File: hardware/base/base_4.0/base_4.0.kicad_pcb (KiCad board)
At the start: 2 copper layers, 94.6 x 17 mm, 9 parts, among them IC1 single_pad_smd, IC2 single_pad_smd, J1 Conn 1, J2 Conn 2

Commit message: 3.0 and 3.5 base updated
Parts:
- removed GND (x2): single_pad_smd, cycfi_library:single-pad-3x2
- removed IC1, IC2, OC1, OC2: single_pad_smd, cycfi_library:single-pad-2x2-th
- added J3: Conn_01x03, cycfi_library:xr2-coil-connector, F.Cu at (125.0, 52.0)
- added J4: Conn_01x03, cycfi_library:xr2-coil-connector, F.Cu at (125.0, 58.5)
- moved J1 6.00 mm to (156.5, 55.2)
- moved J2 5.70 mm to (153.1, 55.2)
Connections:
- net /ic2 renamed /OC2
- net /oc1 renamed /OC1
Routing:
- net GND: track 100.3 -> 9.22 mm, vias 6 -> 2
- net /ic1: track 34.3 -> 0.00 mm
- net /OC2: track 16.2 -> 32.6 mm
- net /OC1: track 56.5 -> 42.8 mm
- net /IC1: track 0.00 -> 10.2 mm
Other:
- outline, holes or cut-outs redrawn
- board text removed: "IC1"
- board text removed: "IC2"
- board text removed: "OC1"
- board text removed: "OC2"

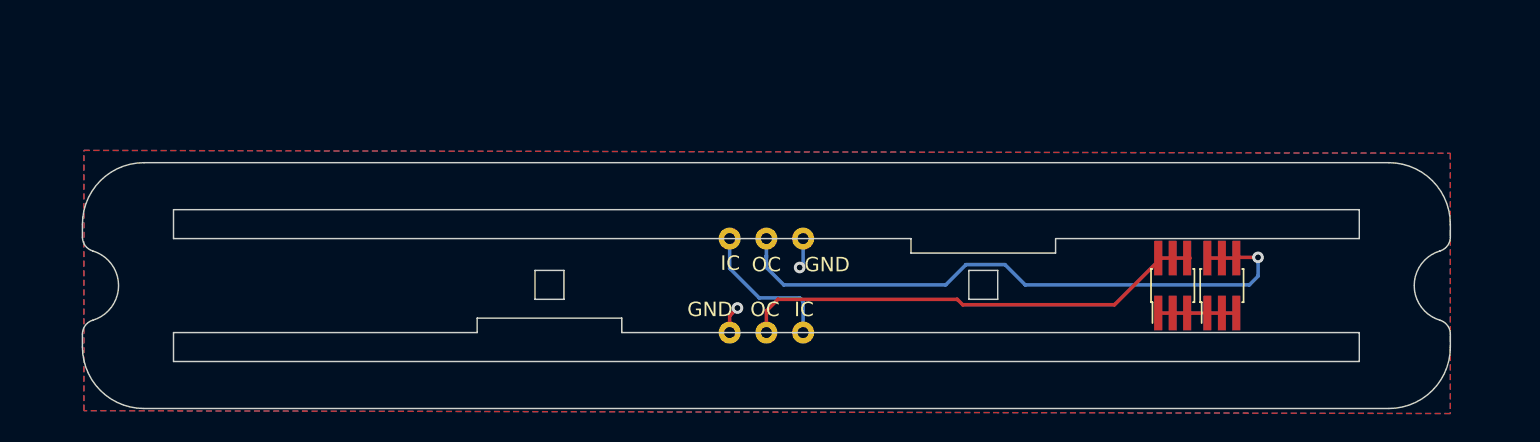
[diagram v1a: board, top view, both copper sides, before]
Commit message: Copied 3.3 to 3.5 and 4.0
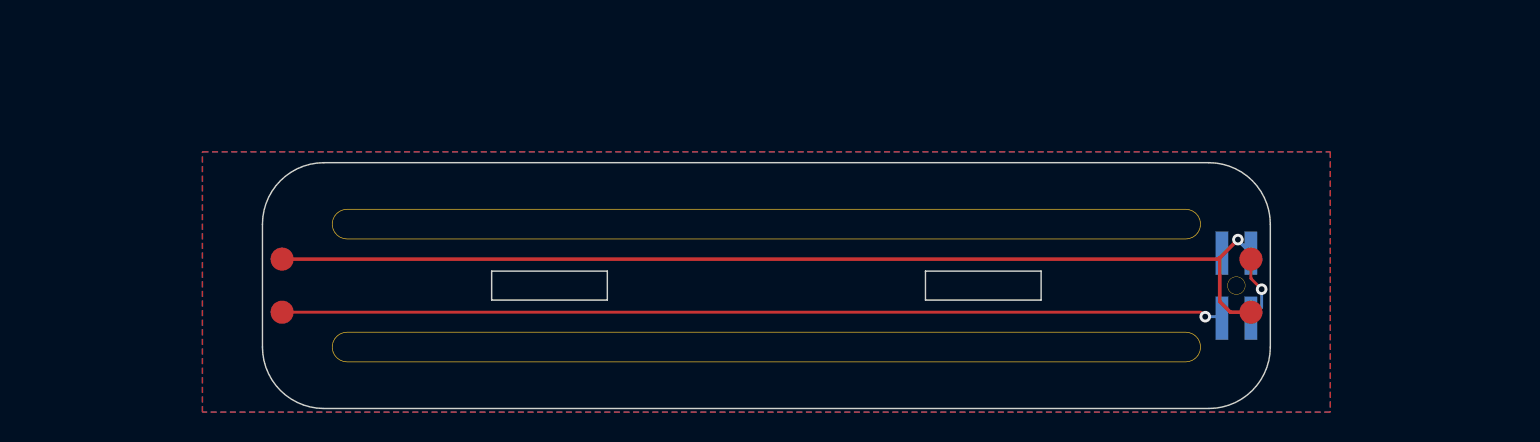
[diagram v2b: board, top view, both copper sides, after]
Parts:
- removed J2: Conn 2, cycfi_library:pin_header_2x3p_1.00mm_smd_vertical
- removed J3, J4: Conn_01x03, cycfi_library:xr2-coil-connector
- added H5: single_pad, xr_spectra_library:rail_slot_3.3, F.Cu at (125.0, 51.0)
- added H6: single_pad, xr_spectra_library:rail_slot_3.3, F.Cu at (125.0, 59.5)
- added IC1: single_pad, cycfi_library:single-pad-1.6x1.6_circular, F.Cu at (91.5, 53.4)
- added IC2: single_pad, cycfi_library:single-pad-1.6x1.6_circular, F.Cu at (158.5, 57.1)
- added OC1: single_pad, cycfi_library:single-pad-1.6x1.6_circular, F.Cu at (158.5, 53.4)
- added OC2: single_pad, cycfi_library:single-pad-1.6x1.6_circular, F.Cu at (91.5, 57.1)
- J1: value Conn 1 -> conn_2x2; footprint cycfi_library:pin_header_2x3p_1.00mm_smd_vertical -> cycfi_library:pin_header_2x2p_2.00mm_smd_vertical; moved to B.Cu
- moved J1 1.00 mm to (157.5, 55.2)
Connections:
- J1 pad 1: GND -> inner_coil
- J1 pad 3: GND -> /out-
- J1 pad 4: /OC1 -> /out+
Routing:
- net inner_coil: track 0.00 -> 73.4 mm, vias 0 -> 1
- net /out-: track 0.00 -> 65.2 mm, vias 0 -> 1
- net /OC1: track 42.8 -> 0.00 mm, vias 1 -> 0
- net /OC2: track 32.6 -> 0.00 mm
- net /IC1: track 10.2 -> 0.00 mm
- net GND: track 9.22 -> 0.00 mm, vias 2 -> 0
- net /out+: track 0.00 -> 4.70 mm, vias 0 -> 1
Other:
- board size 94.6 x 17 mm -> 69.7 x 17 mm
- net class Default removed

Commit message: WIP
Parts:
- added H1: MountingHole, cycfi_library:hole_3mm, F.Cu at (138.0, 39.0)
- added H2: MountingHole, cycfi_library:hole_3mm, F.Cu at (134.0, 39.0)
- H5, H6: footprint xr_spectra_library:rail_slot_3.3 -> xr_spectra_library:rail_slot_4.0
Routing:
- net inner_coil: track 73.4 -> 0.00 mm, vias 1 -> 0
- net /out-: track 65.2 -> 0.00 mm, vias 1 -> 0
- net /out+: track 4.70 -> 0.00 mm, vias 1 -> 0
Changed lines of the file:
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@@
   (footprint "cycfi_library:single-pad-1.6x1.6_circular" (layer "F.Cu")
     (at 158.51 57.09 180)
-    (property "Sheetfile" "base_3.3.kicad_sch")
+    (property "Sheetfile" "base_4.0.kicad_sch")
     (property "Sheetname" "")
     (attr smd)
@@
   (footprint "cycfi_library:single-pad-1.6x1.6_circular" (layer "F.Cu")
     (at 91.51 57.09 180)
-    (property "Sheetfile" "base_3.3.kicad_sch")
+    (property "Sheetfile" "base_4.0.kicad_sch")
     (property "Sheetname" "")
     (attr smd)
@@
   (footprint "cycfi_library:single-pad-1.6x1.6_circular" (layer "F.Cu")
     (at 158.51 53.42 180)
-    (property "Sheetfile" "base_3.3.kicad_sch")
+    (property "Sheetfile" "base_4.0.kicad_sch")
     (property "Sheetname" "")
     (attr smd)
@@
   (footprint "cycfi_library:single-pad-1.6x1.6_circular" (layer "F.Cu")
     (at 91.51 53.42 180)
-    (property "Sheetfile" "base_3.3.kicad_sch")
+    (property "Sheetfile" "base_4.0.kicad_sch")
     (property "Sheetname" "")
     (attr smd)
@@
       (net 2 "inner_coil") (pinfunction "1") (pintype "input"))
   )
-  (footprint "xr_spectra_library:rail_slot_3.3" (layer "F.Cu")
+  (footprint "xr_spectra_library:rail_slot_4.0" (layer "F.Cu")
     (at 125 59.5)
-    (property "Sheetfile" "base_3.3.kicad_sch")
+    (property "Sheetfile" "base_4.0.kicad_sch")
     (property "Sheetname" "")
     (attr through_hole)
@@
       (effects (font (size 1 1) (thickness 0.15)))
     )
-    (pad "1" thru_hole oval (at 0 0) (size 60.1 2.1) (drill oval 60 2) (layers *.Cu *.Mask)
+    (pad "1" thru_hole oval (at 0 0) (size 80.15 2.15) (drill oval 80 2) (layers *.Cu *.Mask)
       (net 1 "GND") (pinfunction "1") (pintype "input"))
   )
-  (footprint "xr_spectra_library:rail_slot_3.3" (layer "F.Cu")
+  (footprint "cycfi_library:hole_3mm" (layer "F.Cu")
+    (at 138 39)
+    (descr "Mounting Hole 2.1mm, no annular")
+    (tags "mounting hole 2.1mm no annular")
+    (property "Sheetfile" "base_4.0.kicad_sch")
+    (property "Sheetname" "")
+    (attr exclude_from_pos_files)
+    (fp_text reference "H1" (at 0 -3.2) (layer "F.SilkS") hide
+      (effects (font (size 1 1) (thickness 0.15)))
+    )
+    (fp_text value "MountingHole" (at 0 3.2) (layer "F.Fab")
+      (effects (font (size 1 1) (thickness 0.15)))
+    )
+    (fp_text user "${REFERENCE}" (at 0.3 0) (layer "F.Fab")
+      (effects (font (size 1 1) (thickness 0.15)))
+    )
+    (fp_circle (center 0 0) (end 0.6 0) (layer "F.CrtYd") (width 0.05) (fill none))
+    (pad "" np_thru_hole circle (at 0 0) (size 3 3) (drill 3) (layers F&B.Cu *.Mask))
+  )
+  (footprint "xr_spectra_library:rail_slot_4.0" (layer "F.Cu")
     (at 125 51)
-    (property "Sheetfile" "base_3.3.kicad_sch")
+    (property "Sheetfile" "base_4.0.kicad_sch")
     (property "Sheetname" "")
     (attr through_hole)
@@
       (effects (font (size 1 1) (thickness 0.15)))
     )
-    (pad "1" thru_hole oval (at 0 0) (size 60.1 2.1) (drill oval 60 2) (layers *.Cu *.Mask)
+    (pad "1" thru_hole oval (at 0 0) (size 80.15 2.15) (drill oval 80 2) (layers *.Cu *.Mask)
       (net 1 "GND") (pinfunction "1") (pintype "input"))
+  )
+  (footprint "cycfi_library:hole_3mm" (layer "F.Cu")
+    (at 134 39)
+    (descr "Mounting Hole 2.1mm, no annular")
+    (tags "mounting hole 2.1mm no annular")
+    (property "Sheetfile" "base_4.0.kicad_sch")
+    (property "Sheetname" "")
+    (attr exclude_from_pos_files)
+    (fp_text reference "H2" (at 0 -3.2) (layer "F.SilkS") hide
+      (effects (font (size 1 1) (thickness 0.15)))
+    )
+    (fp_text value "MountingHole" (at 0 3.2) (layer "F.Fab")
+      (effects (font (size 1 1) (thickness 0.15)))
+    )
+    (fp_text user "${REFERENCE}" (at 0.3 0) (layer "F.Fab")
+      (effects (font (size 1 1) (thickness 0.15)))
+    )
+    (fp_circle (center 0 0) (end 0.6 0) (layer "F.CrtYd") (width 0.05) (fill none))
+    (pad "" np_thru_hole circle (at 0 0) (size 3 3) (drill 3) (layers F&B.Cu *.Mask))
   )
   (footprint "cycfi_library:cycfi-logo-15mm" locked (layer "B.Cu")
@@
     (descr "surface-mounted straight pin socket, 2x2, 2.00mm pitch, double rows")
     (tags "Surface mounted pin header SMD 2x2 200mm double row")
-    (property "Sheetfile" "base_3.3.kicad_sch")
+    (property "Sheetfile" "base_4.0.kicad_sch")
     (property "Sheetname" "")
     (attr smd)
@@
   (gr_arc (start 155.6 46.75) (mid 158.605204 47.994796) (end 159.85 51) (layer "Edge.Cuts") (width 0.1))
   (gr_line (start 106 56.25) (end 114 56.25) (layer "Edge.Cuts") (width 0.1))
-  (segment (start 156.35 53.33024) (end 157.610262 52.069978) (width 0.25) (layer "F.Cu") (net 2))
-  (segment (start 157.09 57.09) (end 156.35 56.35) (width 0.25) (layer "F.Cu") (net 2))
-  (segment (start 156.35 56.35) (end 156.35 53.33024) (width 0.25) (layer "F.Cu") (net 2))
-  (segment (start 91.51 53.42) (end 156.26024 53.42) (width 0.25) (layer "F.Cu") (net 2))
-  (segment (start 156.26024 53.42) (end 156.35 53.33024) (width 0.25) (layer "F.Cu") (net 2))
-  (segment (start 158.51 57.09) (end 157.09 57.09) (width 0.25) (layer "F.Cu") (net 2))
-  (via (at 157.610262 52.069978) (size 0.8) (drill 0.4) (layers "F.Cu" "B.Cu") (net 2))
-  (segment (start 157.610262 52.110262) (end 158.5 53) (width 0.25) (layer "B.Cu") (net 2))
-  (segment (start 157.610262 52.069978) (end 157.610262 52.110262) (width 0.25) (layer "B.Cu") (net 2))
-  (segment (start 155.04 57.09) (end 155.35 57.4) (width 0.2) (layer "F.Cu") (net 3))
-  (segment (start 91.51 57.09) (end 155.04 57.09) (width 0.2) (layer "F.Cu") (net 3))
-  (via (at 155.35 57.4) (size 0.8) (drill 0.4) (layers "F.Cu" "B.Cu") (net 3))
-  (segment (start 155.35 57.4) (end 156.4 57.4) (width 0.2) (layer "B.Cu") (net 3))
-  (segment (start 156.4 57.4) (end 156.5 57.5) (width 0.2) (layer "B.Cu") (net 3))
-  (segment (start 158.51 54.76) (end 159.25 55.5) (width 0.2) (layer "F.Cu") (net 4))
-  (segment (start 158.51 53.42) (end 158.51 54.76) (width 0.2) (layer "F.Cu") (net 4))
-  (via (at 159.25 55.5) (size 0.8) (drill 0.4) (layers "F.Cu" "B.Cu") (net 4))
-  (segment (start 159.25 56.75) (end 158.5 57.5) (width 0.2) (layer "B.Cu") (net 4))
-  (segment (start 159.25 55.5) (end 159.25 56.75) (width 0.2) (layer "B.Cu") (net 4))
   (zone (net 1) (net_name "GND") (layer "F.Cu") (hatch edge 0.508)
     (connect_pads yes (clearance 0.508))
     (min_thickness 0.254) (filled_areas_thickness no)
-    (fill yes (thermal_gap 0.508) (thermal_bridge_width 0.508))
+    (fill (thermal_gap 0.508) (thermal_bridge_width 0.508))
     (polygon
       (pts
@@
     (connect_pads yes (clearance 0.508))
     (min_thickness 0.254) (filled_areas_thickness no)
-    (fill yes (thermal_gap 0.508) (thermal_bridge_width 0.508))
+    (fill (thermal_gap 0.508) (thermal_bridge_width 0.508))
     (polygon
       (pts

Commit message: 4.0" PCB layout
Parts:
- G***: moved to F.Cu
- moved IC1 79.0 mm to (79.8, 50.5), turned to 0 degrees
- moved OC1 79.0 mm to (170.2, 50.5), turned to 0 degrees
- moved OC2 79.0 mm to (79.8, 59.0), turned to 0 degrees
- moved IC2 78.9 mm to (170.2, 59.0), turned to 0 degrees
- moved J1 76.0 mm to (81.5, 54.8), turned to -90 degrees
- moved H1 62.3 mm to (77.7, 54.8), turned to 180 degrees
- moved H2 41.4 mm to (172.3, 54.8), turned to 180 degrees
- moved H6 9.00 mm to (125.0, 50.5)
- moved H5 8.00 mm to (125.0, 59.0)
- moved G*** 0.71 mm to (124.8, 54.8), turned to 0 degrees
- renumbered IC2 to IC1, IC1 to IC2, OC2 to OC1, OC1 to OC2
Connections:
- IC1 pad 1: inner_coil -> /out+
- IC2 pad 1: inner_coil -> /out-
- J1 pad 1: inner_coil -> middle_coil
- OC1 pad 1: /out- -> middle_coil
- OC2 pad 1: /out+ -> middle_coil
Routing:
- net middle_coil: track 0.00 -> 104.1 mm, vias 0 -> 1
- net /out-: track 0.00 -> 91.3 mm, vias 0 -> 1
- net /out+: track 0.00 -> 3.66 mm, vias 0 -> 1
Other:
- board size 69.7 x 17 mm -> 101 x 17 mm

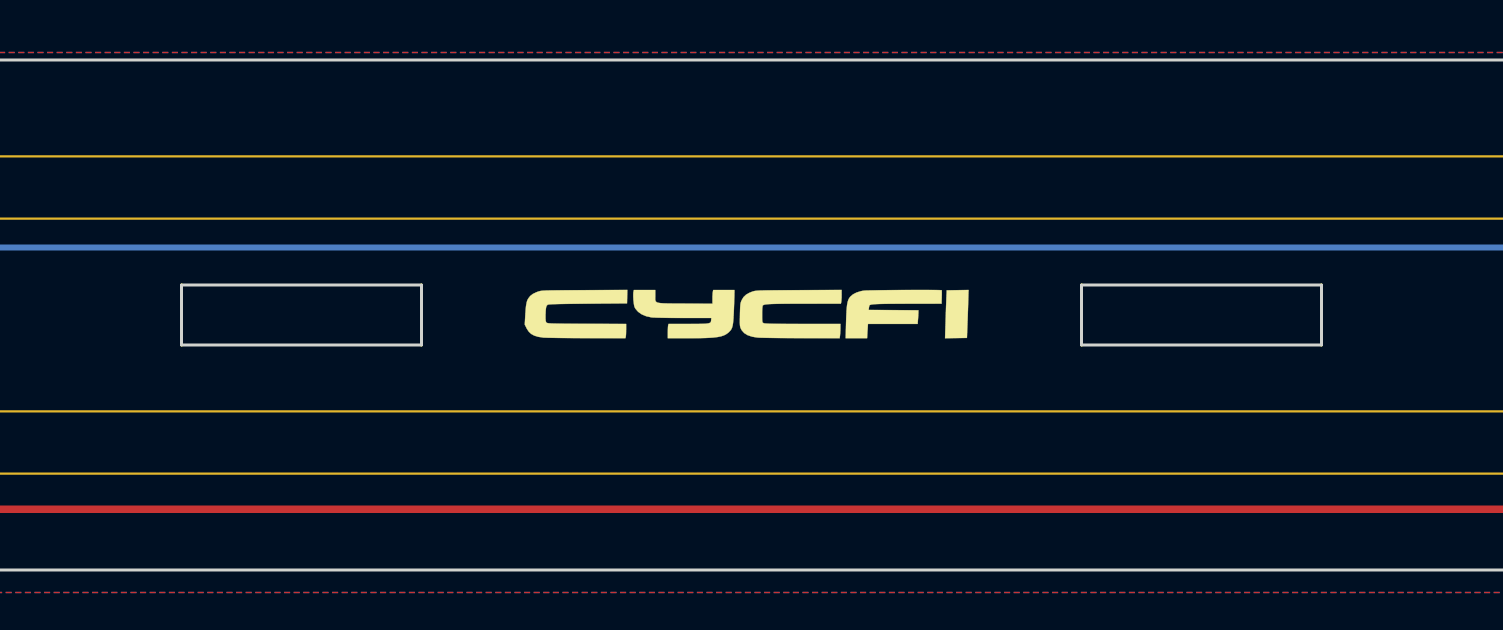
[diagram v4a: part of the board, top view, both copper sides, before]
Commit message: adjusted for proper mouse-bites in panels
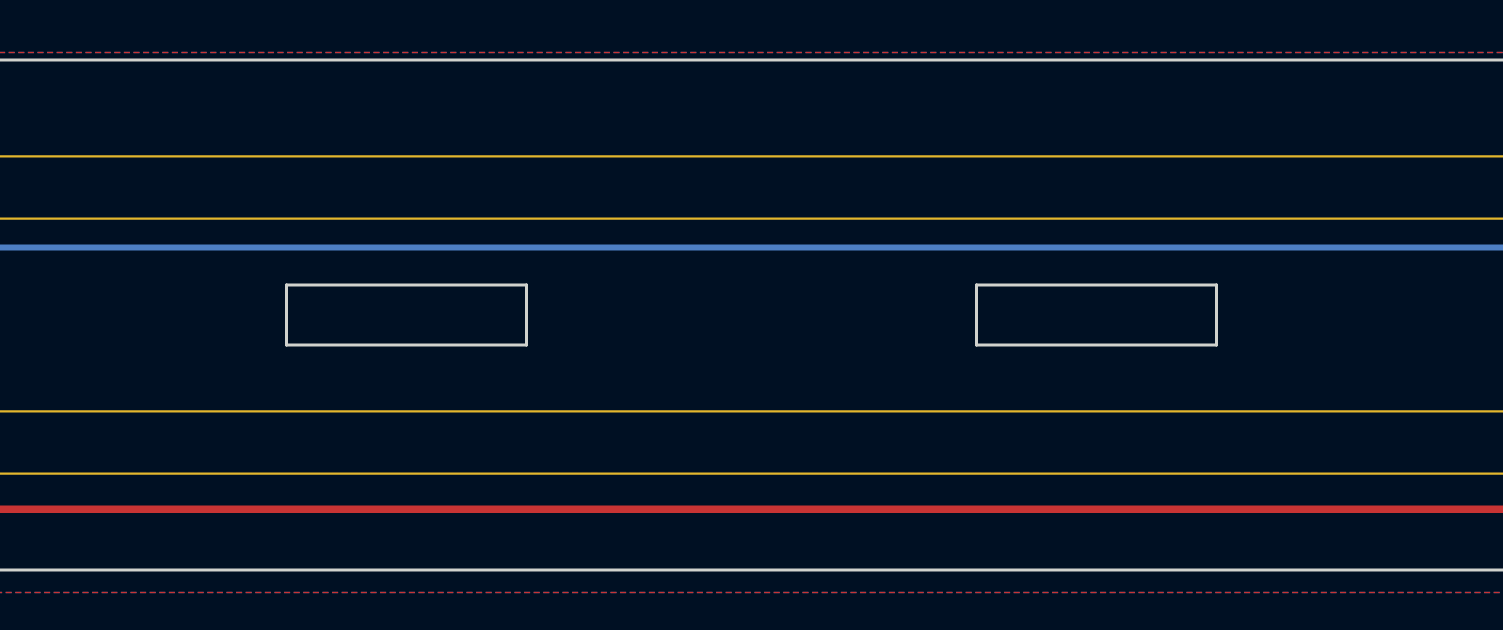
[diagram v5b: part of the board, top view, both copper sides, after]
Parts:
- removed G***: LOGO, cycfi_library:cycfi-logo-15mm
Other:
- outline, holes or cut-outs redrawn
